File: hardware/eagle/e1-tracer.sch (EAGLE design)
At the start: 112 parts, among them IC1 MCP1703T-1202E/CB, IC2 W25Q80DVSNIG, IC3 TLV70233DBVR, IC4 ASEM1-12.000MHZ-LC-T, J1 PASSTHROUGH, M1 MENTOR_12701001, M2 MENTOR_12701001, SW1 TACTSW-TL3340, T1 BC847C, T2 BC847C, U1 ICE40UP5K-SG48I, U2 IP4234CZ6, U3 IP4234CZ6, U4 IDT82V2081, U5 IDT82V2081, U6 2.048 Mhz, U7 1.544 MHz, X1 MINI-USB-SHIELD-UX60-MB-5ST, X2 JACK2.5_SJ-2523

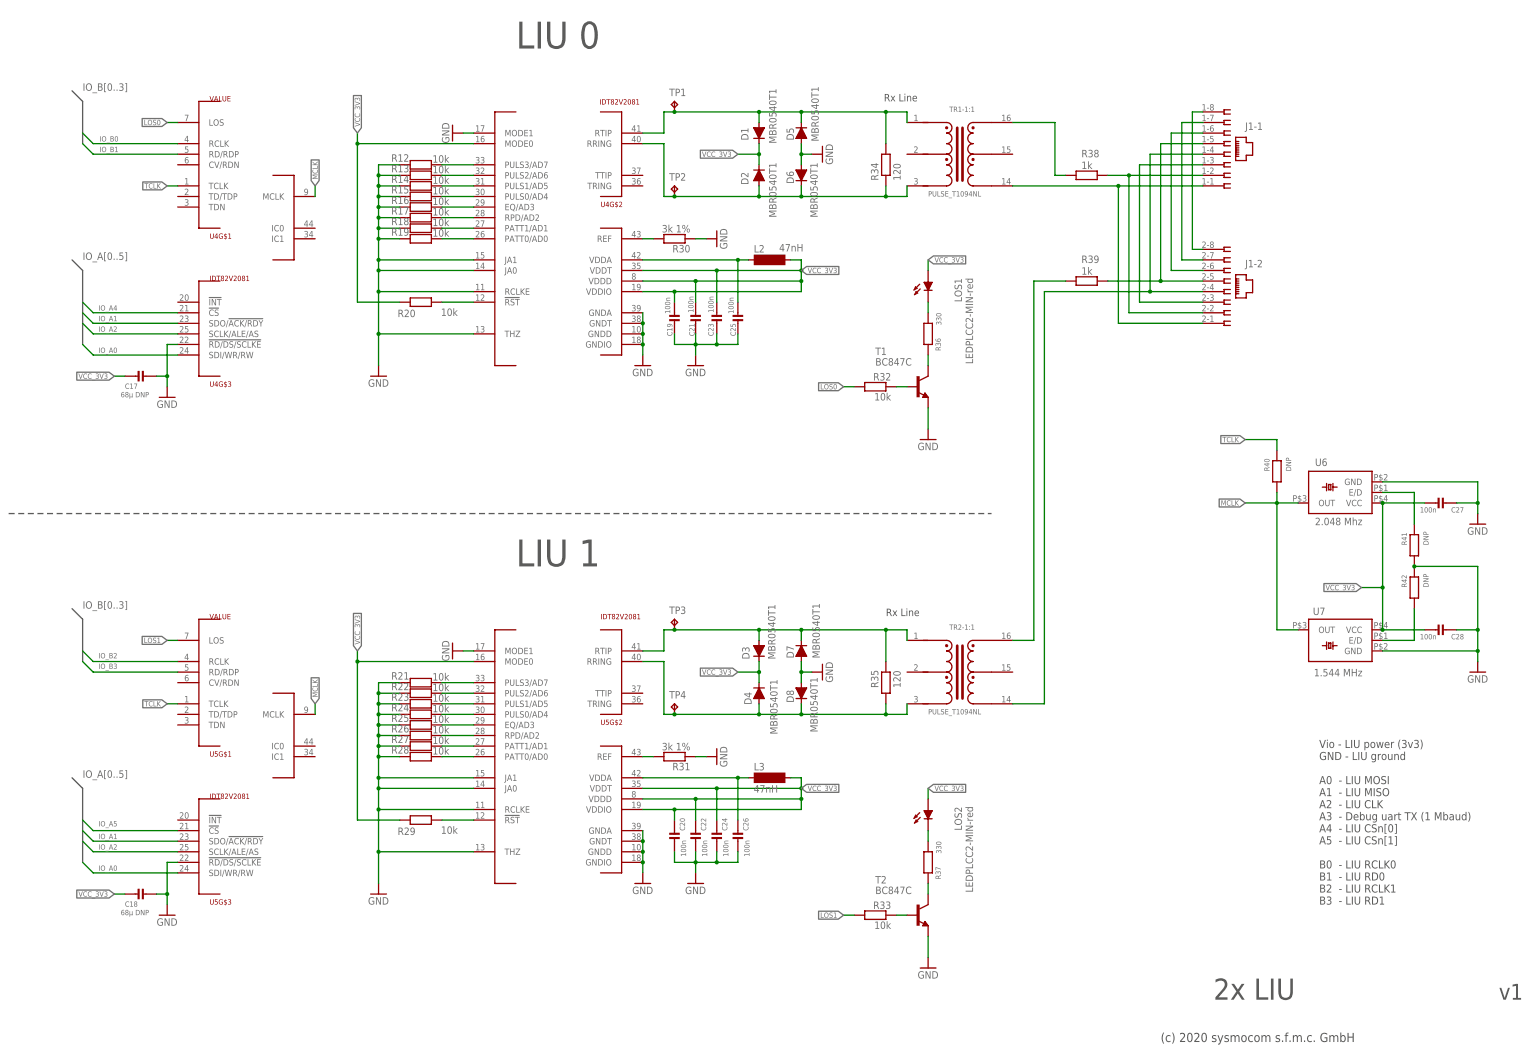
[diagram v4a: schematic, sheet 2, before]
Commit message: e1-tracer: improve power bypassing on LIU's VDDT and VDDA
...by placing 2x 22u per LIU (instead of 68u DNP), shrinking packages
from 1206 to 0805
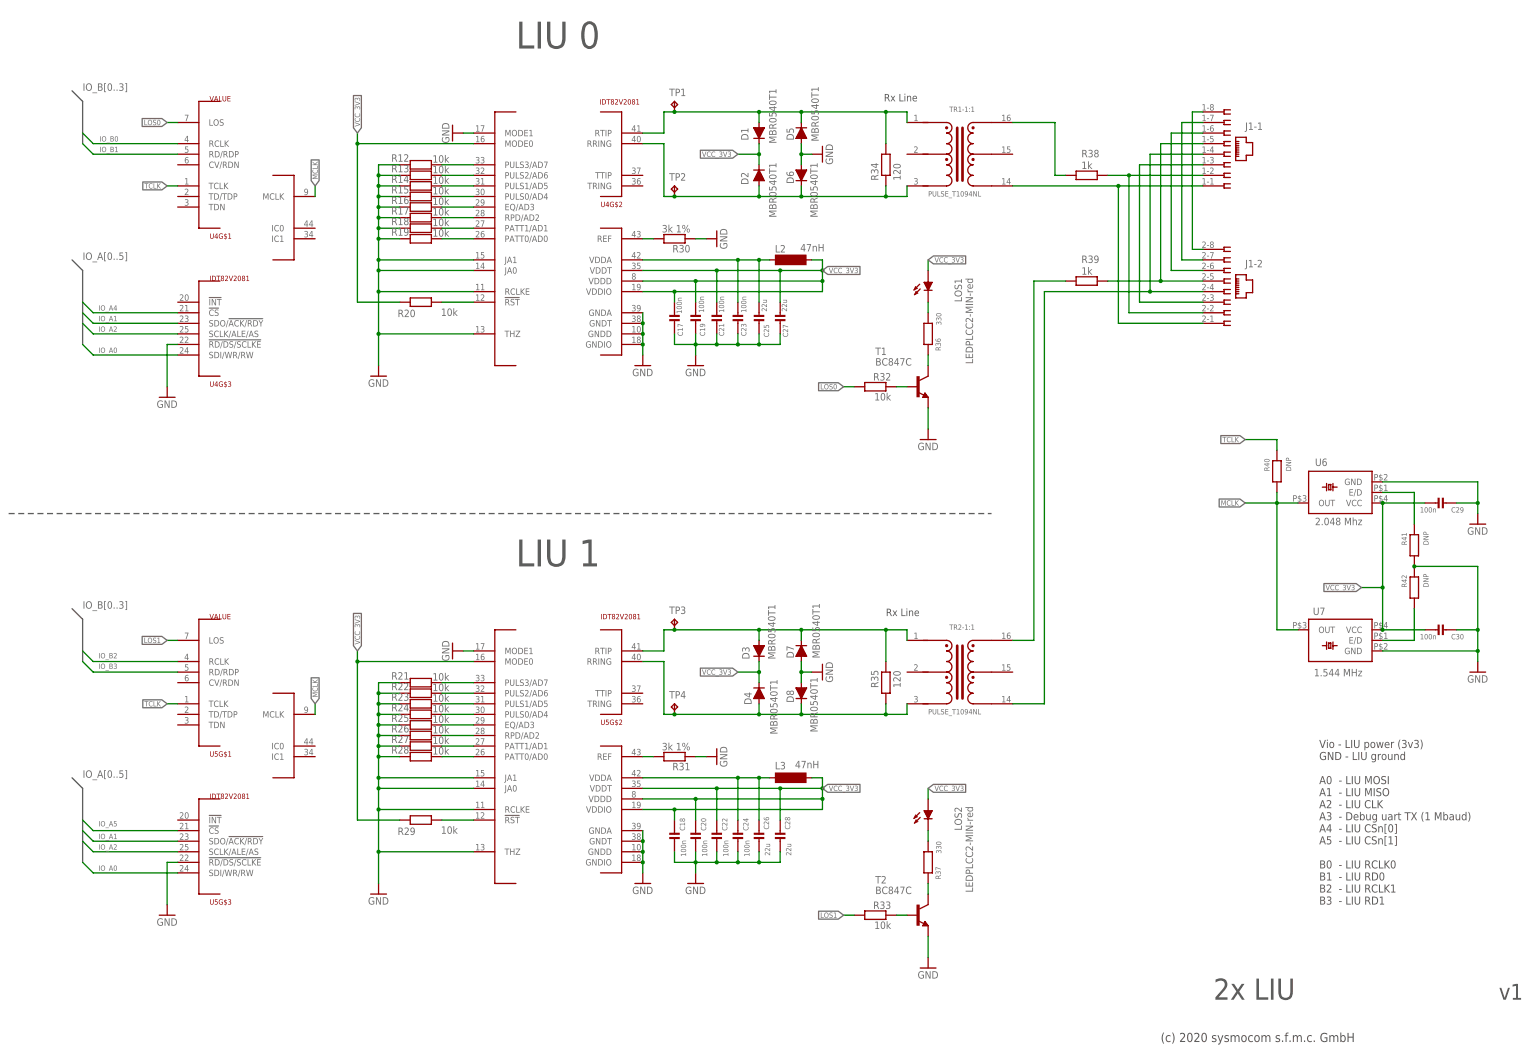
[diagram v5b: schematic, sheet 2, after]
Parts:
- added C29, C30: 100n, rc-sysmocom:CAP_CERAMIC_0603
- C17, C18: value 68µ DNP -> 100n
- C25, C26, C27, C28: value 100n -> 22u; device rc-sysmocom:CAP_CERAMIC_0603 -> rc-sysmocom:CAP_CERAMIC_0805; DESCRIPTION CAP CER 0.1UF 16V 10% X7R 0603 -> NO DESCRIPTION; LINK http://www.digikey.de/product-detail/de/foo/1276-1005-1-ND -> https://www.digikey.de/product-detail/de/kemet/C0805C226M9P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; MANUFACTURER Samsung Electro-Mechanics America, Inc -> UNKNOWN MANUFACTURER; MANUFACTURERPARTNUMBER CL10B104KO8NNNC -> UNKNOWN MANUFACTURER PART NUMBER; ROHSCERTIFICATE Bleifrei / RoHS-konform -> UNKNOWN ROHS CERTIFICATE; SOURCE DIGIKEY -> UNKNOWN SOURCE; SOURCEPARTNUMBER 1276-1005-1-ND -> UNKNOWN SOURCE PART NUMBER
- IC3: CLASS (none) -> UNKNOWN CLASS; DESCRIPTION (none) -> NO DESCRIPTION; LINK (none) -> UNKNOWN LINK; MANUFACTURER (none) -> UNKNOWN MANUFACTURER; MANUFACTURERPARTNUMBER (none) -> UNKNOWN MANUFACTURER PART NUMBER; POPULATED (none) -> TRUE; ROHSCERTIFICATE (none) -> UNKNOWN ROHS CERTIFICATE; SOURCE (none) -> UNKNOWN SOURCE; SOURCEPARTNUMBER (none) -> UNKNOWN SOURCE PART NUMBER
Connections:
- net GND: now also C17.2, C18.2, C25.1, C26.1, C29.1, C30.1; no longer C17.1, C18.1, C25.2, C26.2
- net N$23: now also C23.1, C25.2; no longer C25.1
- net N$3: now also C24.1, C26.2; no longer C26.1
- net VCC_3V3: now also C17.1, C18.1, C29.2, C30.2; no longer C17.2, C18.2, C23.1, C24.1
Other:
- moved on the sheet: C17, C18, C19, C20, C21, C22, C23, C24, C25, C26, C27, C28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

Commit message: e1-tracer: add a generic 0603 blue LED type w/ Vf=2.8V
designating LTST-C193TBKT-5A for now
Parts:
- CDONE: LINK UNKNOWN LINK -> https://www.digikey.de/product-detail/de/lite-on-inc/LTST-C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
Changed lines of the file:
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@@
 <attribute name="CLASS" value="UNKNOWN CLASS"/>
 <attribute name="DESCRIPTION" value="NO DESCRIPTION"/>
-<attribute name="LINK" value="UNKNOWN LINK"/>
+<attribute name="LINK" value="https://www.digikey.de/product-detail/de/lite-on-inc/LTST-C193TBKT-5A/160-1827-1-ND"/>
 <attribute name="MANUFACTURER" value="UNKNOWN MANUFACTURER"/>
 <attribute name="MANUFACTURERPARTNUMBER" value="UNKNOWN MANUFACTURER PART NUMBER"/>
@@
 </busses>
 <nets>
-<net name="GND" class="0">
+<net name="GND" class="1">
 <segment>
 <pinref part="GND4" gate="1" pin="GND"/>
@@
 </busses>
 <nets>
-<net name="GND" class="0">
+<net name="GND" class="1">
 <segment>
 <wire x1="104.14" y1="215.9" x2="104.14" y2="213.36" width="0.1524" layer="91"/>

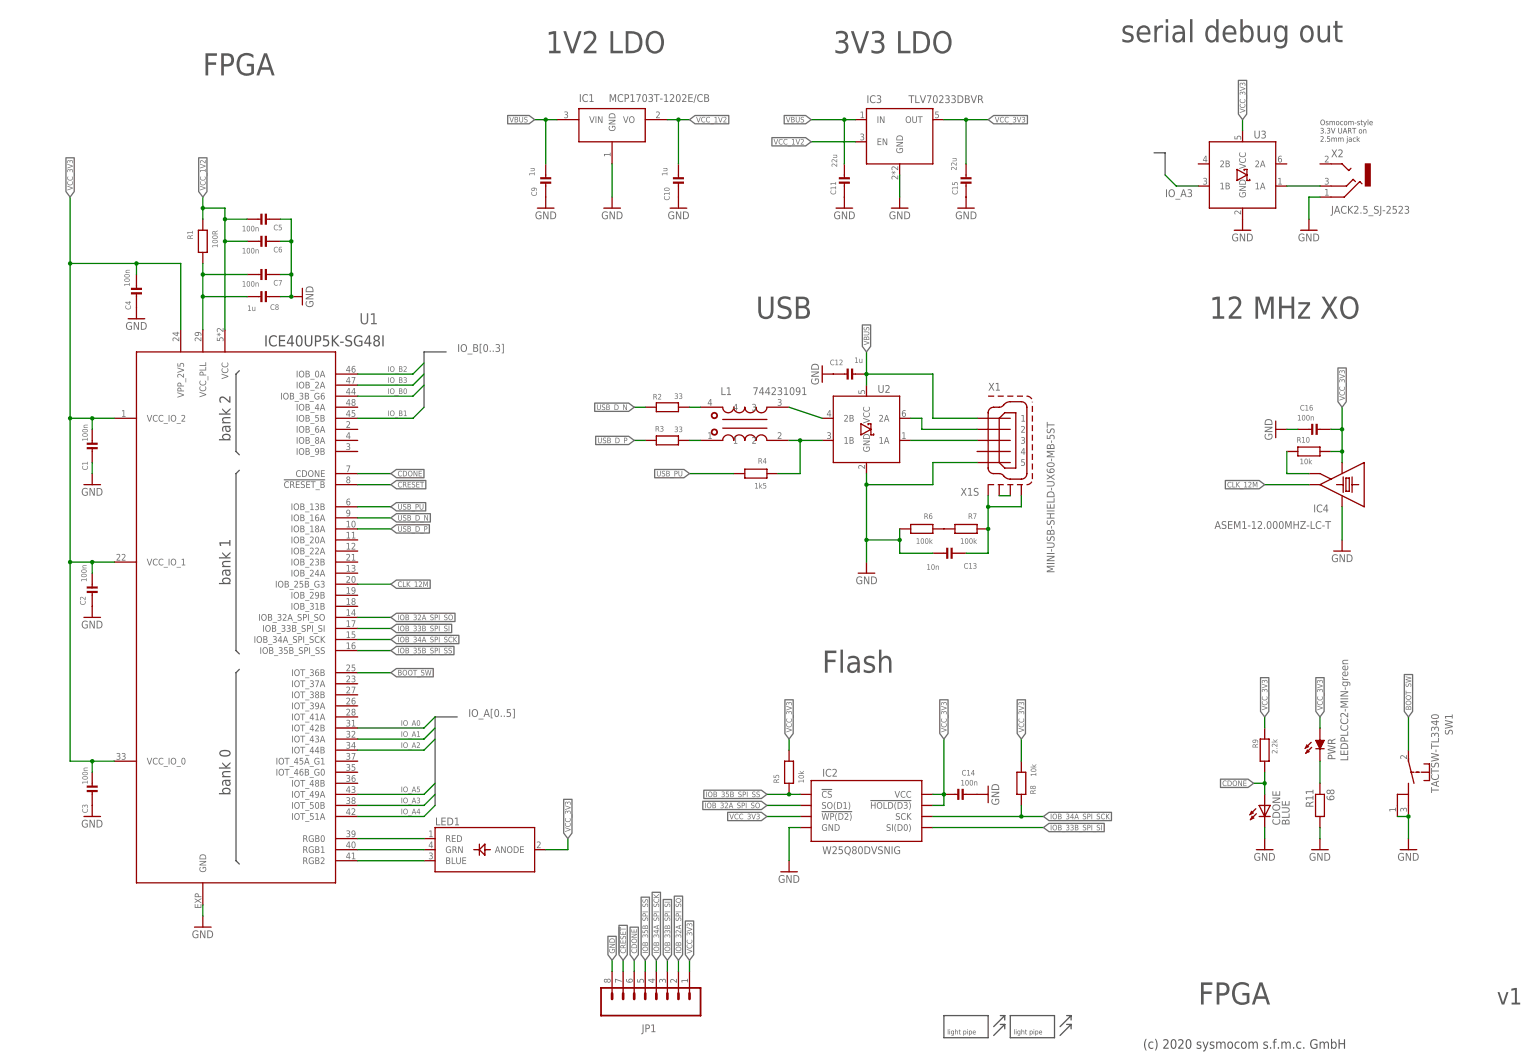
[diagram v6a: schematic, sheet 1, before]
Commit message: e1-tracer: have more clearance of VBUS trace on PCB edge
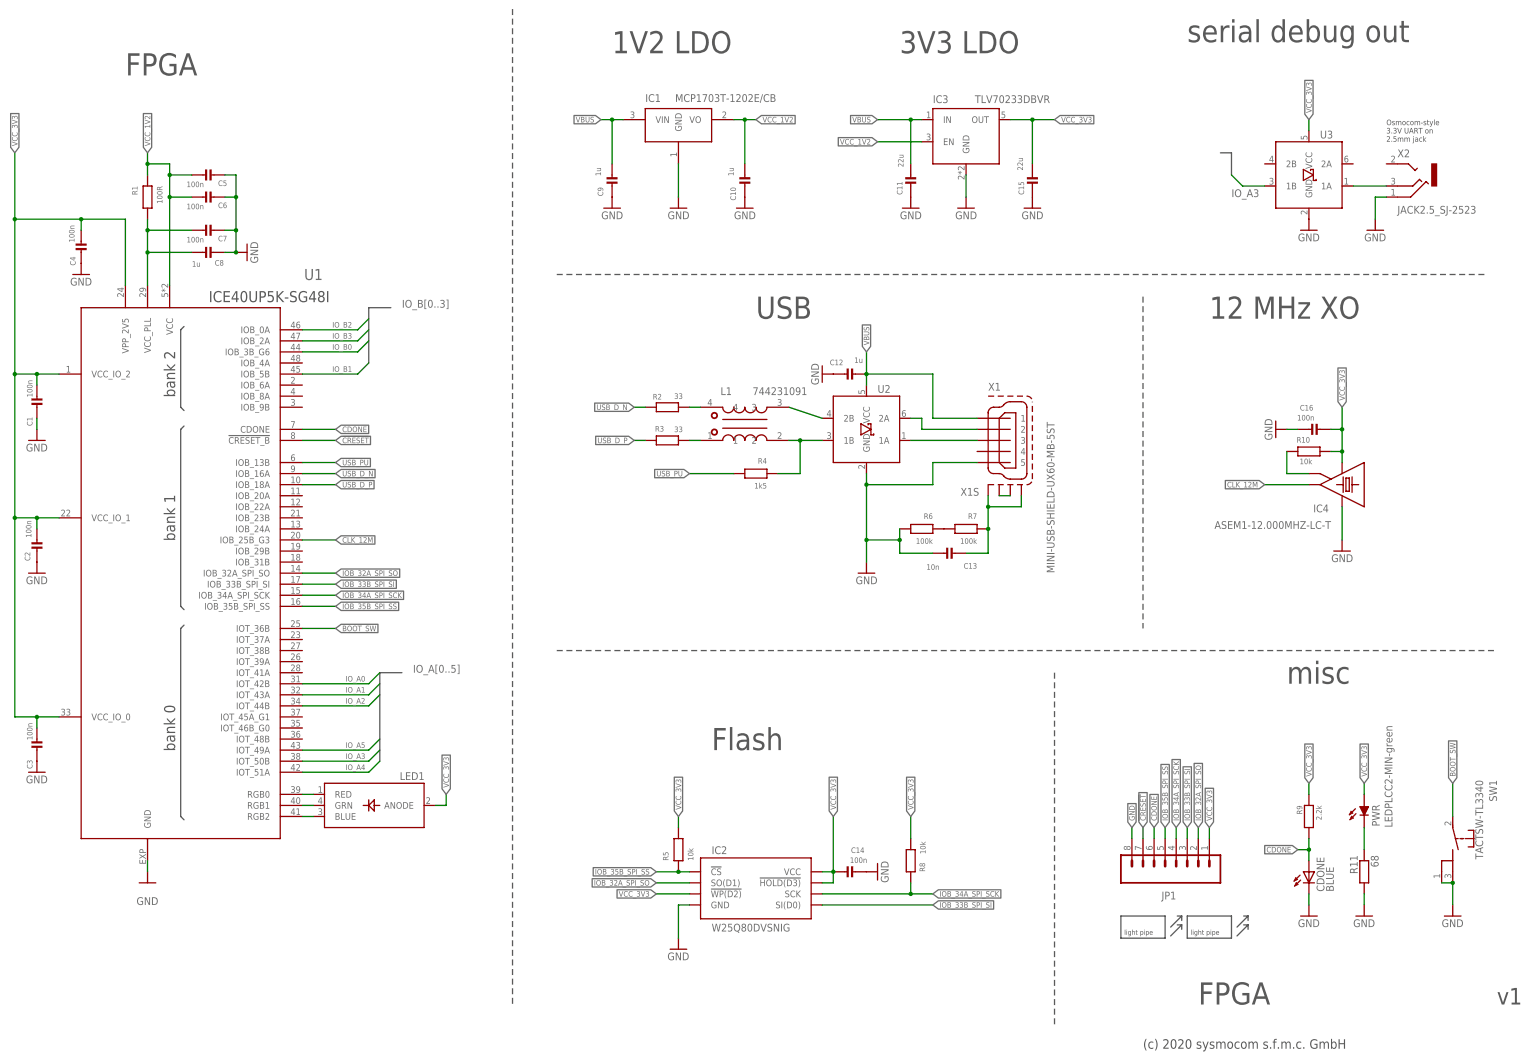
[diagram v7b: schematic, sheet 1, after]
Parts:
- CDONE: device led:LEDCHIPLED_0805 -> led:LEDCHIPLED_0603
- J1: LINK UNKNOWN LINK -> https://www.digikey.de/product-detail/de/te-connectivity-am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; SOURCEPARTNUMBER UNKNOWN SOURCE PART NUMBER -> A31449-ND
- M1, M2: MANUFACTURER UNKNOWN MANUFACTURER -> Mentor
- R9: device rc-sysmocom:RESISTOR_0402 -> rc-sysmocom:RESISTOR_0603; DESCRIPTION RES 2.20K OHM 1/16W 1% 0402 SMD -> NO DESCRIPTION; LINK http://www.digikey.de/product-detail/de/RC0402FR-072K2L/311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 -> UNKNOWN LINK; MANUFACTURER Yageo -> UNKNOWN MANUFACTURER; MANUFACTURERPARTNUMBER RC0402FR-072K2L -> UNKNOWN MANUFACTURER PART NUMBER; ROHSCERTIFICATE Bleifrei / RoHS-konform -> UNKNOWN ROHS CERTIFICATE; SOURCE DIGIKEY -> UNKNOWN SOURCE; SOURCEPARTNUMBER 311-2.20KLRCT-ND -> UNKNOWN SOURCE PART NUMBER
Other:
- note added: "misc"
- moved on the sheet: C1, C10, C11, C14, C15, C2, C3, C4, C5, C6, C7, C8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

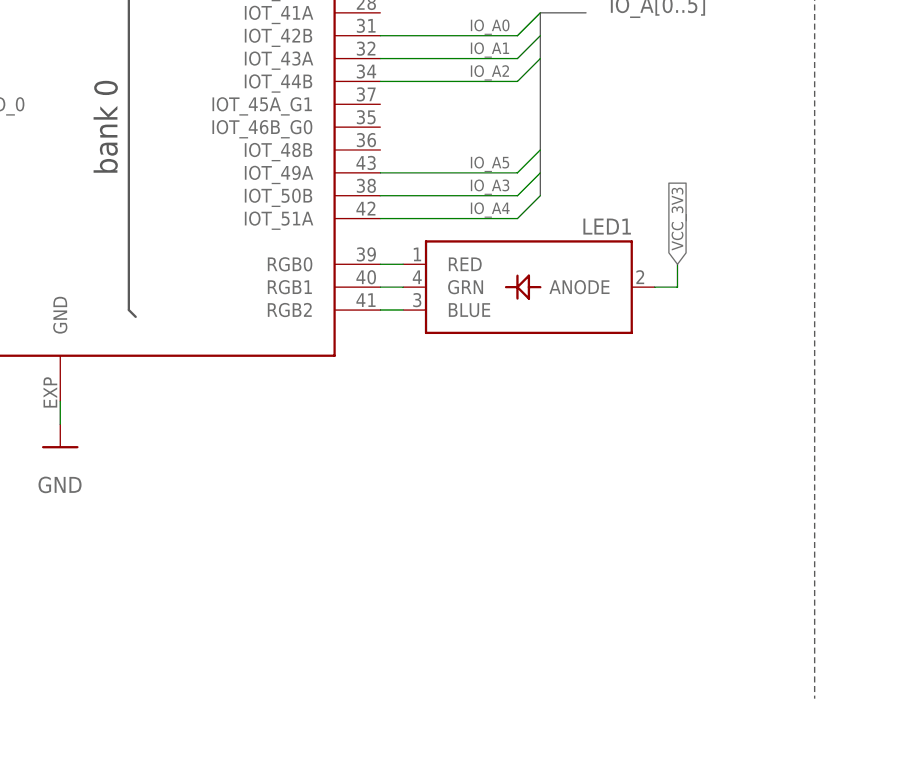
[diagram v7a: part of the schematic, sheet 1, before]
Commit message: e1-tracer: 4x 0R on R and B LED color selection wires
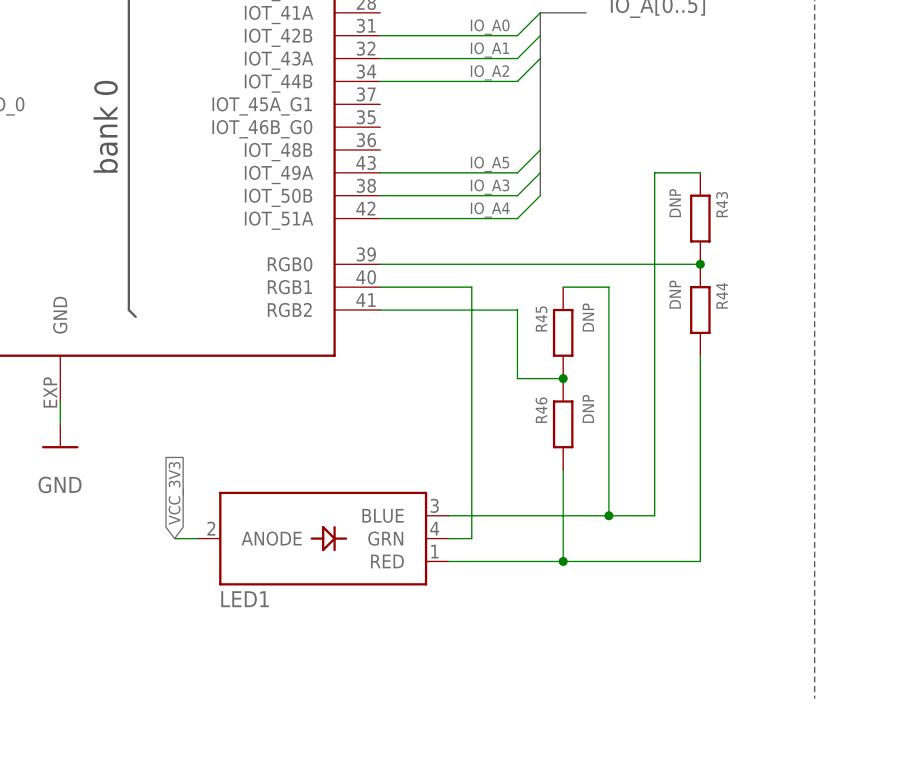
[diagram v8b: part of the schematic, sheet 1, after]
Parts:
- removed LOS2: LEDPLCC2-MIN-red, LED-PLCC2:LEDPLCC2-MIN
- added LOS0: LEDPLCC2-MIN-red, LED-PLCC2:LEDPLCC2-MIN
- added R43, R44, R45, R46: DNP, rc-sysmocom:RESISTOR_0603
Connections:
- new net N$45: R45.2, R46.1, U1.RGB2
- new net N$46: LED1.RED, R44.2, R46.2
- net N$27: now also LOS0.C; no longer LOS1.C
- net N$37: now also LOS1.C; no longer LOS2.C
- net N$63: now also R43.2, R44.1; no longer LED1.RED
- net N$65: now also R43.1, R45.1; no longer U1.RGB2
- net VCC_3V3: now also LOS0.A; no longer LOS2.A
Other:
- moved on the sheet: LED1, LOS1
